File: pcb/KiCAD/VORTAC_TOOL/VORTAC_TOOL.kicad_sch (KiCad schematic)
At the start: 6 parts, among them J1 Conn_01x05, J2 Conn_01x02, J3 Conn_01x03

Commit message: Check Lcsc numbers
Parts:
- J1, J2, J3: now left out of the parts list
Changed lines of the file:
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@@
 		(unit 1)
 		(exclude_from_sim no)
-		(in_bom yes)
+		(in_bom no)
 		(on_board yes)
 		(dnp no)
@@
 		(unit 1)
 		(exclude_from_sim no)
-		(in_bom yes)
+		(in_bom no)
 		(on_board yes)
 		(dnp no)
@@
 		(unit 1)
 		(exclude_from_sim no)
-		(in_bom yes)
-		(on_board yes)
-		(dnp no)
+		(in_bom no)
+		(on_board yes)
+		(dnp no)

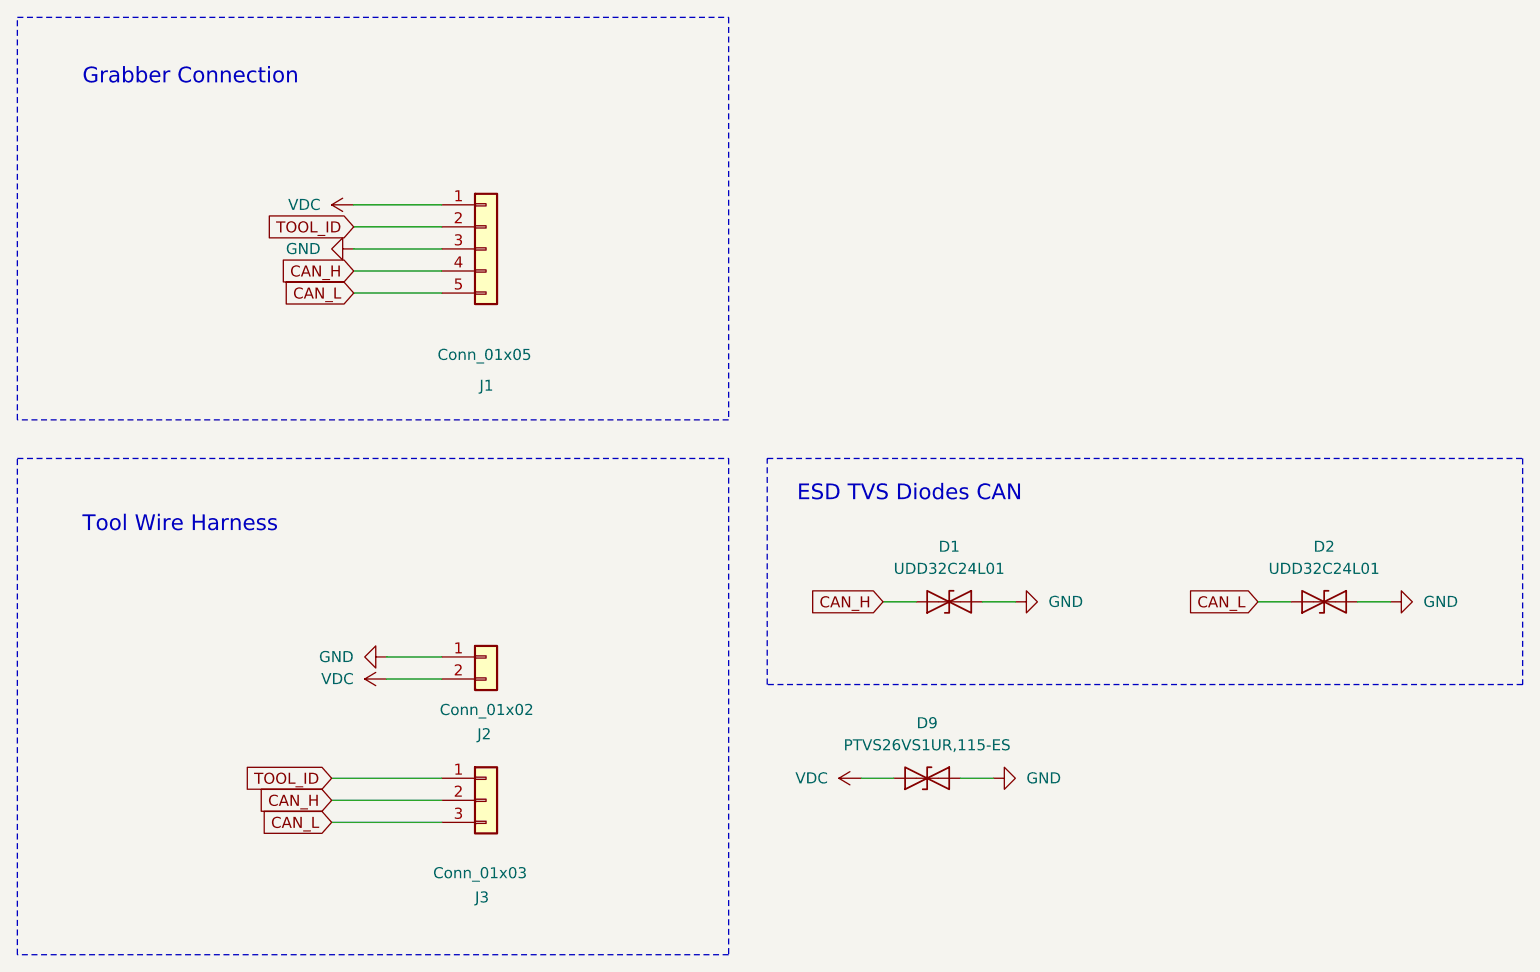
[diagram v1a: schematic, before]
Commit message: updateting Custom Foorprints to show Ref**
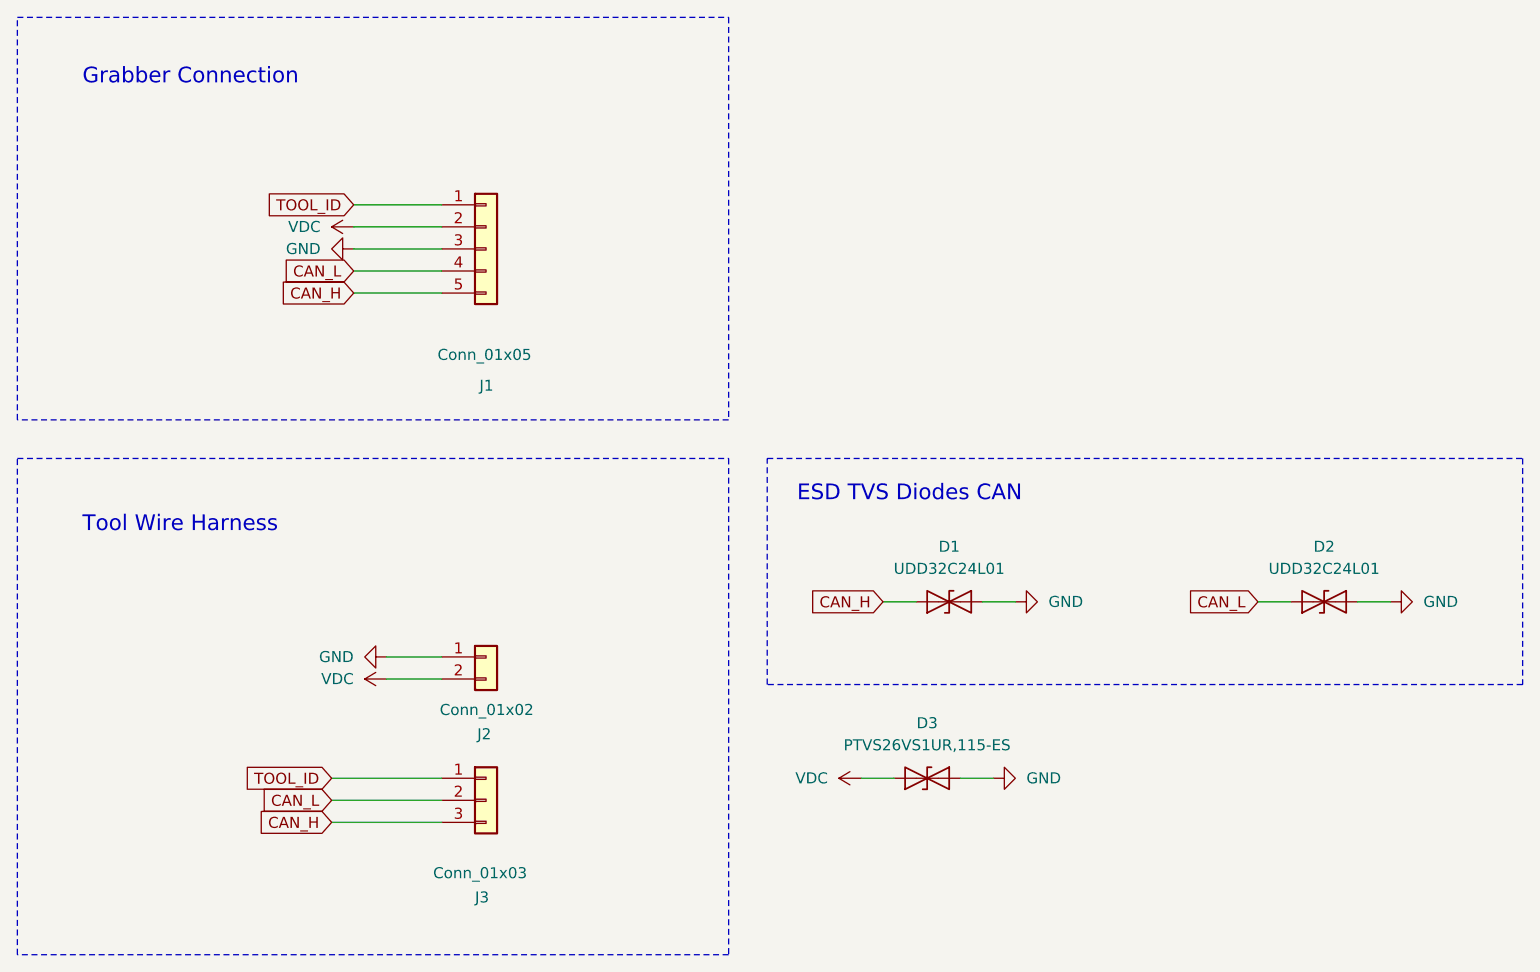
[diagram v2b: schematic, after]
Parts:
- renumbered D9 to D3
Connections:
- net CAN_H: now also J1.5 (Pin_5), J3.3 (Pin_3); no longer J1.4 (Pin_4), J3.2 (Pin_2)
- net CAN_L: now also J1.4 (Pin_4), J3.2 (Pin_2); no longer J1.5 (Pin_5), J3.3 (Pin_3)
- net TOOL_ID: now also J1.1 (Pin_1); no longer J1.2 (Pin_2)
- net VDC: now also J1.2 (Pin_2); no longer J1.1 (Pin_1)
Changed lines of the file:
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@@
 	(global_label "CAN_H"
 		(shape input)
-		(at 58.42 48.26 180)
+		(at 58.42 50.8 180)
 		(fields_autoplaced yes)
 		(effects
@@
 		)
 		(property "Intersheetrefs" "${INTERSHEET_REFS}"
-			(at 49.4476 48.26 0)
+			(at 49.4476 50.8 0)
 			(effects
 				(font
@@
 	(global_label "CAN_H"
 		(shape input)
-		(at 55.88 109.22 180)
+		(at 55.88 111.76 180)
 		(fields_autoplaced yes)
 		(effects
@@
 		)
 		(property "Intersheetrefs" "${INTERSHEET_REFS}"
-			(at 46.9076 109.22 0)
+			(at 46.9076 111.76 0)
 			(effects
 				(font
@@
 	(global_label "CAN_L"
 		(shape input)
-		(at 58.42 50.8 180)
+		(at 58.42 48.26 180)
 		(fields_autoplaced yes)
 		(effects
@@
 		)
 		(property "Intersheetrefs" "${INTERSHEET_REFS}"
-			(at 49.75 50.8 0)
+			(at 49.75 48.26 0)
 			(effects
 				(font
@@
 	(global_label "TOOL_ID"
 		(shape input)
-		(at 58.42 43.18 180)
+		(at 58.42 40.64 180)
 		(fields_autoplaced yes)
 		(effects
@@
 		)
 		(property "Intersheetrefs" "${INTERSHEET_REFS}"
-			(at 47.9357 43.18 0)
+			(at 47.9357 40.64 0)
 			(effects
 				(font
@@
 	(global_label "CAN_L"
 		(shape input)
-		(at 55.88 111.76 180)
+		(at 55.88 109.22 180)
 		(fields_autoplaced yes)
 		(effects
@@
 		)
 		(property "Intersheetrefs" "${INTERSHEET_REFS}"
-			(at 47.21 111.76 0)
+			(at 47.21 109.22 0)
 			(effects
 				(font
@@
 		(dnp no)
 		(fields_autoplaced yes)
-		(property "Reference" "#PWR09"
+		(property "Reference" "#PWR03"
 			(at 140.97 86.36 0)
 			(effects
@@
 			(project "VORTAC_TOOLPLATE_REV1"
 				(path "/b23b3086-82ed-4285-9d49-d03b4e41a1a0"
-					(reference "#PWR09")
+					(reference "#PWR03")
 					(unit 1)
 				)
@@
 		(dnp no)
 		(fields_autoplaced yes)
-		(property "Reference" "#PWR010"
+		(property "Reference" "#PWR04"
 			(at 184.15 86.36 0)
 			(effects
@@
 			(project "VORTAC_TOOLPLATE_REV1"
 				(path "/b23b3086-82ed-4285-9d49-d03b4e41a1a0"
-					(reference "#PWR010")
+					(reference "#PWR04")
 					(unit 1)
 				)
@@
 		(dnp no)
 		(fields_autoplaced yes)
-		(property "Reference" "D9"
+		(property "Reference" "D3"
 			(at 124.46 100.33 0)
 			(effects
@@
 			(project "VORTAC_TOOLPLATE_REV1"
 				(path "/b23b3086-82ed-4285-9d49-d03b4e41a1a0"
-					(reference "D9")
+					(reference "D3")
 					(unit 1)
 				)
@@
 		(dnp no)
 		(fields_autoplaced yes)
-		(property "Reference" "#PWR01"
+		(property "Reference" "#PWR02"
 			(at 52.07 45.72 0)
 			(effects
@@
 			(project ""
 				(path "/b23b3086-82ed-4285-9d49-d03b4e41a1a0"
-					(reference "#PWR01")
+					(reference "#PWR02")
 					(unit 1)
 				)
@@
 		(dnp no)
 		(fields_autoplaced yes)
-		(property "Reference" "#PWR012"
+		(property "Reference" "#PWR08"
 			(at 138.43 106.68 0)
 			(effects
@@
 			(project "VORTAC_TOOLPLATE_REV1"
 				(path "/b23b3086-82ed-4285-9d49-d03b4e41a1a0"
-					(reference "#PWR012")
+					(reference "#PWR08")
 					(unit 1)
 				)
@@
 		(dnp no)
 		(fields_autoplaced yes)
-		(property "Reference" "#PWR011"
+		(property "Reference" "#PWR07"
 			(at 120.65 106.68 0)
 			(effects
@@
 			(project "VORTAC_TOOLPLATE_REV1"
 				(path "/b23b3086-82ed-4285-9d49-d03b4e41a1a0"
-					(reference "#PWR011")
+					(reference "#PWR07")
 					(unit 1)
 				)
@@
 	(symbol
 		(lib_id "power:VDC")
-		(at 58.42 40.64 90)
+		(at 58.42 43.18 90)
 		(unit 1)
 		(exclude_from_sim no)
@@
 		(dnp no)
 		(fields_autoplaced yes)
-		(property "Reference" "#PWR02"
-			(at 62.23 40.64 0)
+		(property "Reference" "#PWR01"
+			(at 62.23 43.18 0)
 			(effects
 				(font
@@
 		)
 		(property "Value" "VDC"
-			(at 54.61 40.6399 90)
+			(at 54.61 43.1799 90)
 			(effects
 				(font
@@
 		)
 		(property "Footprint" ""
-			(at 58.42 40.64 0)
+			(at 58.42 43.18 0)
 			(effects
 				(font
@@
 		)
 		(property "Datasheet" ""
-			(at 58.42 40.64 0)
+			(at 58.42 43.18 0)
 			(effects
 				(font
@@
 		)
 		(property "Description" "Power symbol creates a global label with name \"VDC\""
-			(at 58.42 40.64 0)
+			(at 58.42 43.18 0)
 			(effects
 				(font
@@
 			(project ""
 				(path "/b23b3086-82ed-4285-9d49-d03b4e41a1a0"
-					(reference "#PWR02")
-					(unit 1)
-				)
+					(reference "#PWR01")
+					(unit 1)
+				)
